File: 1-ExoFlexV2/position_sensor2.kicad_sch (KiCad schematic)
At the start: 21 parts, among them J103 Jumper, J104 Jumper, J105 Jumper, U73 Inverter, U74 Inverter, U75 Inverter, U76 AND Gate, U77 AND Gate, U78 Inverter

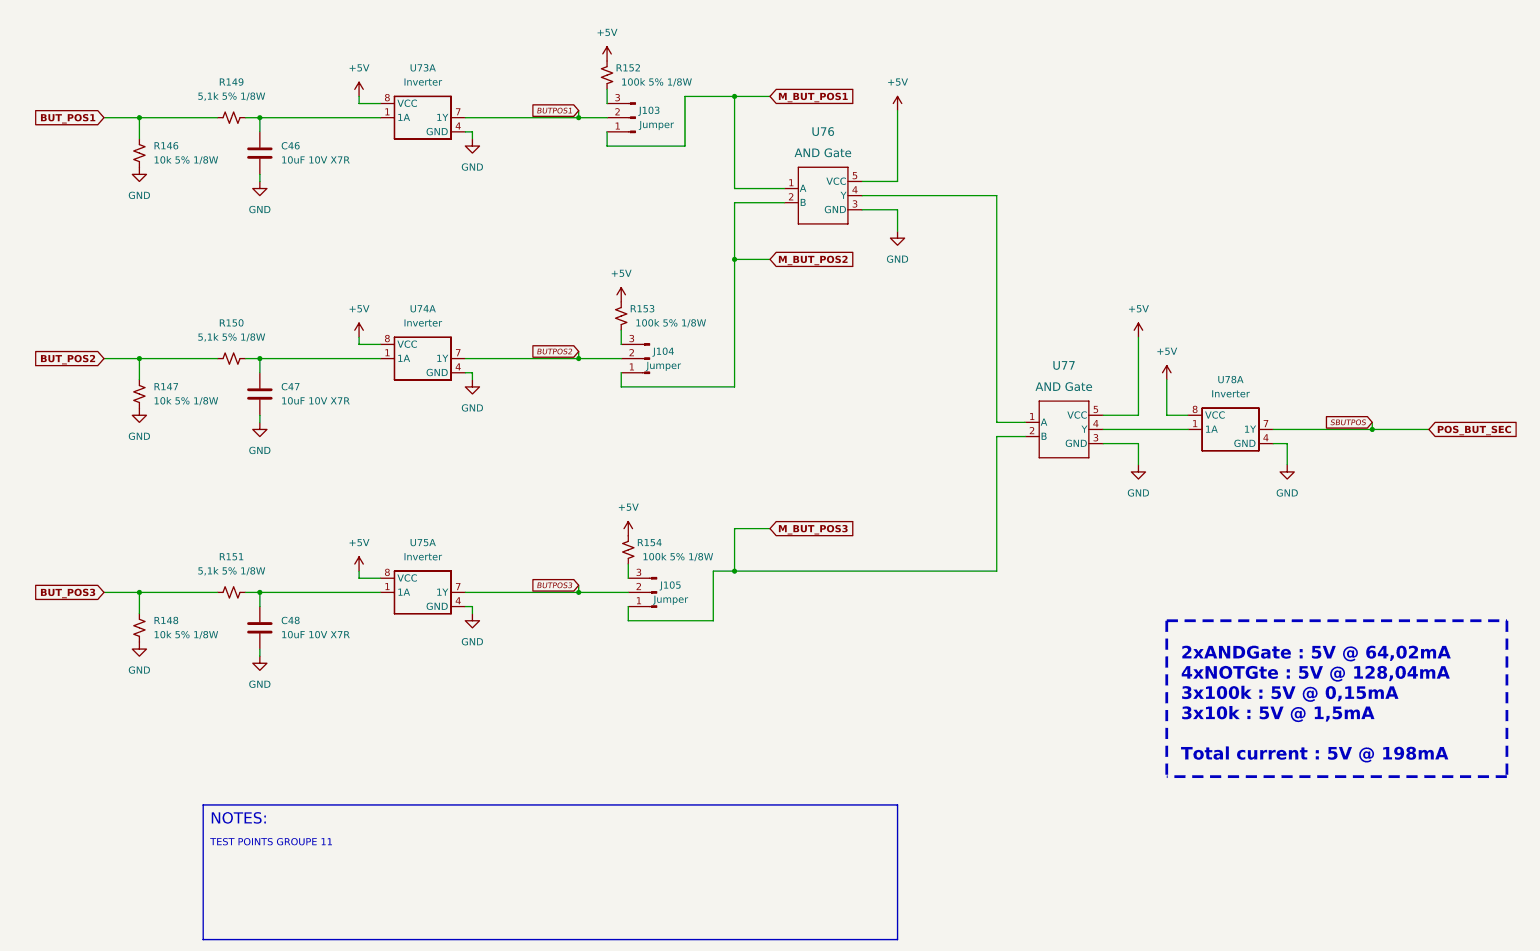
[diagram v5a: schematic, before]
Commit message: Finalisation 3
- Changement des régulateur de tension
- Retrait de test point inutile
- Changement de jumper mal positionner
- Ajout de Mounting holes et fiducial
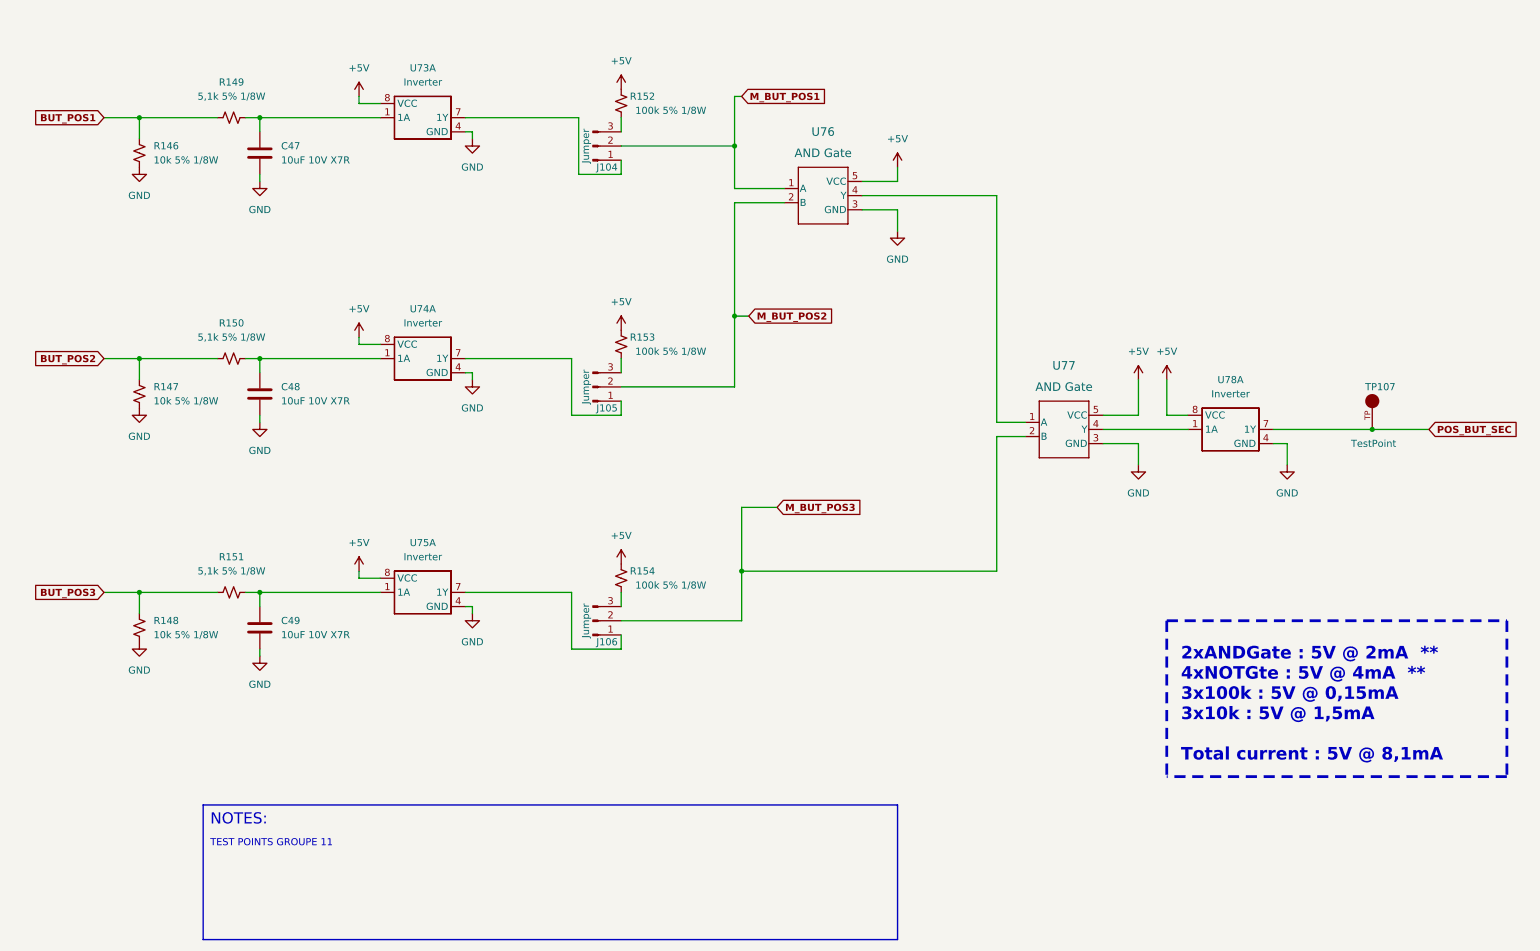
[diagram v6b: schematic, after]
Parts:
- added TP107: TestPoint, FootPrint:KEYSTONE_5005, symbol SymLib:5005
- J104: renamed from J103; footprint Connector_PinSocket_2.54mm:PinSocket_1x03_P2.54mm_Vertical -> Connector_PinHeader_2.54mm:PinHeader_1x03_P2.54mm_Vertical
- J105: renamed from J104; footprint Connector_PinSocket_2.54mm:PinSocket_1x03_P2.54mm_Vertical -> Connector_PinHeader_2.54mm:PinHeader_1x03_P2.54mm_Vertical
- J106: renamed from J105; footprint Connector_PinSocket_2.54mm:PinSocket_1x03_P2.54mm_Vertical -> Connector_PinHeader_2.54mm:PinHeader_1x03_P2.54mm_Vertical
- renumbered C46 to C47, C47 to C48, C48 to C49
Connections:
- net M_BUT_POS1: now also J104.2 (Pin_2); no longer J104.1 (Pin_1)
- net M_BUT_POS2: now also J105.2 (Pin_2); no longer J105.1 (Pin_1)
- net M_BUT_POS3: now also J106.2 (Pin_2); no longer J106.1 (Pin_1)
- net POS_BUT_SEC: now also TP107.TP
- net BUTPOS1: no longer names the net of U73.7 (1Y)
- net BUTPOS1: now also J104.1 (Pin_1); no longer J104.2 (Pin_2)
- net BUTPOS2: no longer names the net of U74.7 (1Y)
- net BUTPOS2: now also J105.1 (Pin_1); no longer J105.2 (Pin_2)
- net BUTPOS3: no longer names the net of U75.7 (1Y)
- net BUTPOS3: now also J106.1 (Pin_1); no longer J106.2 (Pin_2)
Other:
- note added: "2xANDGate : 5V @ 2mA ** 4xNOTGte : 5V @ 4mA ** 3x100k : 5V @ 0,15mA 3x10k : 5V @ 1,5mA Total current : 5V @ 8,1mA"
- note removed: "2xANDGate : 5V @ 64,02mA 4xNOTGte : 5V @ 128,04mA 3x100k : 5V @ 0,15mA 3x10k : 5V @ 1,5mA Total current : 5V @ 198mA"
- moved on the sheet: J104, J105, J106, R152, R153, R154

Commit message: Finalisation schéma FIN
- Changement des uméro pour les inverseurs
- Changement des connecteur et début de placement
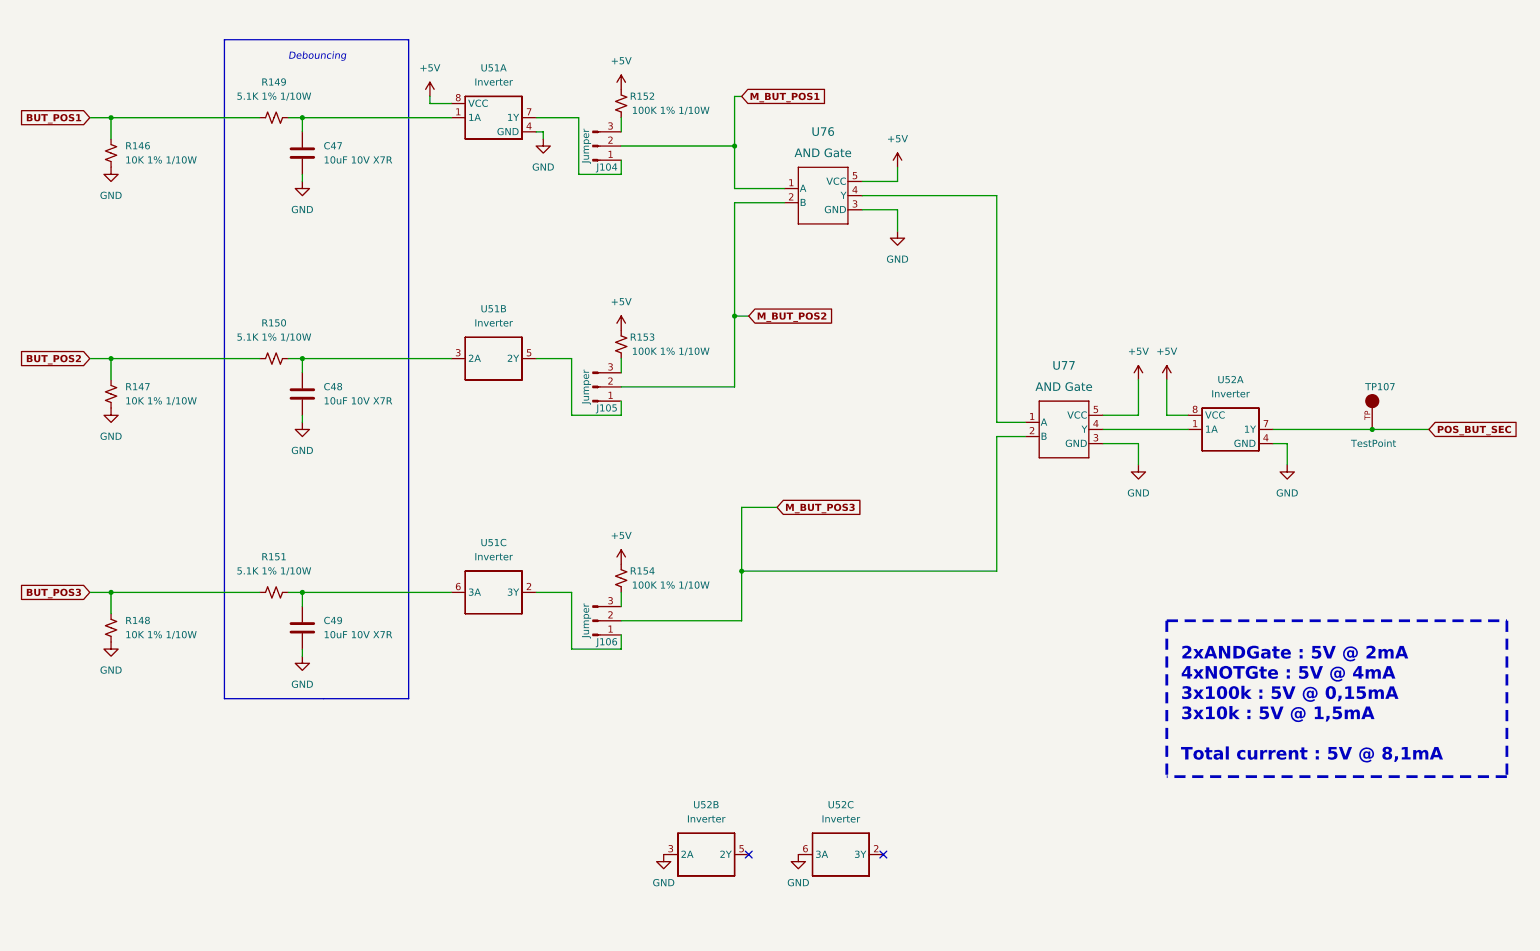
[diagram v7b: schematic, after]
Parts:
- removed U73, U74, U75, U78: Inverter, FootPrint:SN74LVC3G14DCUT, symbol SymLib:SN74LVC3G14DCUT_V2
- added U51, U52: Inverter, FootPrint:SN74LVC3G14DCUT, symbol SymLib:SN74LVC3G14DCUT_V2
- R146, R147, R148: value 10k 5% 1/8W -> 10K 1% 1/10W; footprint Resistor_SMD:R_0805_2012Metric -> Resistor_SMD:R_0603_1608Metric; DESCRIPTION 10 kOhms ±5% 0.125W, 1/8W Chip Resistor 0805 (2012 Metric) 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 -> 10 kOhms ±1% 0.1W, 1/10W Chip Resistor 0603 (1608 Metric) A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; PACKAGE 0805 (2012 Metric) -> 0603 (1608 Metric); PART NUMBER ERJ-6GEYJ103V -> ERJ-3EKF1002V
- R149, R150, R151: value 5,1k 5% 1/8W -> 5.1K 1% 1/10W; footprint Resistor_SMD:R_0805_2012Metric -> Resistor_SMD:R_0603_1608Metric; DESCRIPTION 5.1 kOhms ±5% 0.125W, 1/8W Chip Resistor 0805 (2012 Metric)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 -> 5.1 kOhms ±1% 0.1W, 1/10W Chip Resistor 0603 (1608 Metric) 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; PACKAGE 0805 (2012 Metric) -> 0603 (1608 Metric); PART NUMBER ERJ-6GEYJ512V -> ERJ-3EKF5101V
- R152, R153, R154: value 100k 5% 1/8W -> 100K 1% 1/10W; footprint Resistor_SMD:R_0805_2012Metric -> Resistor_SMD:R_0603_1608Metric; DESCRIPTION 100 kOhms ±5% 0.125W, 1/8W Chip Resistor 0805 (2012 Metric)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 -> 100 kOhms ±1% 0.1W, 1/10W Chip Resistor 0603 (1608 Metric) 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; PACKAGE 0805 (2012 Metric) -> 0603 (1608 Metric); PART NUMBER ERJ-6GEYJ104V -> ERJ-3EKF1003V
- TP107: NOTES (none) -> DO NOT POPULATE; PURCHASE-URL https://pricing.snapeda.com/search/part/5005/?ref=eda -> (none)
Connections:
- net +5V: now also U51.8 (VCC), U52.8 (VCC)
- net GND: now also U51.4 (GND), U52.3 (2A), U52.4 (GND), U52.6 (3A)
- net POS_BUT_SEC: now also U52.7 (1Y)
- net at C48.1, R150.2: now also U51.3 (2A)
- net at J105.1 (Pin_1): now also U51.5 (2Y)
- net at U77.4 (Y): now also U52.1 (1A)
- net at C49.1, R151.2: now also U51.6 (3A)
- net at J104.1 (Pin_1): now also U51.7 (1Y)
- net at C47.1, R149.2: now also U51.1 (1A)
- net at J106.1 (Pin_1): now also U51.2 (3Y)
- no-connect marks 0 -> 2
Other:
- note added: "2xANDGate : 5V @ 2mA 4xNOTGte : 5V @ 4mA 3x100k : 5V @ 0,15mA 3x10k : 5V @ 1,5mA Total current : 5V @ 8,1mA"
- note added: "Debouncing"
- note removed: "2xANDGate : 5V @ 2mA ** 4xNOTGte : 5V @ 4mA ** 3x100k : 5V @ 0,15mA 3x10k : 5V @ 1,5mA Total current : 5V @ 8,1mA"
- note removed: "NOTES:"
- note removed: "TEST POINTS GROUPE 11"
- moved on the sheet: C47, C48, C49, R146, R147, R148, R149, R150, R151

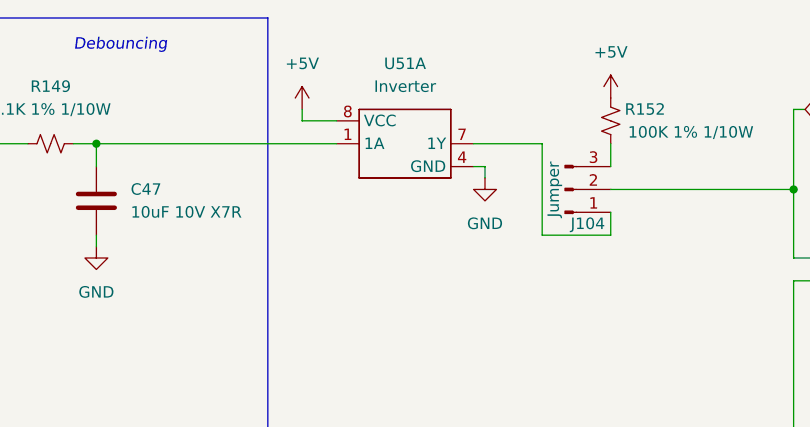
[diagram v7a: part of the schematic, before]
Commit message: Placement 1
- Placement de tous les connecteur
- Placement de tous les test point
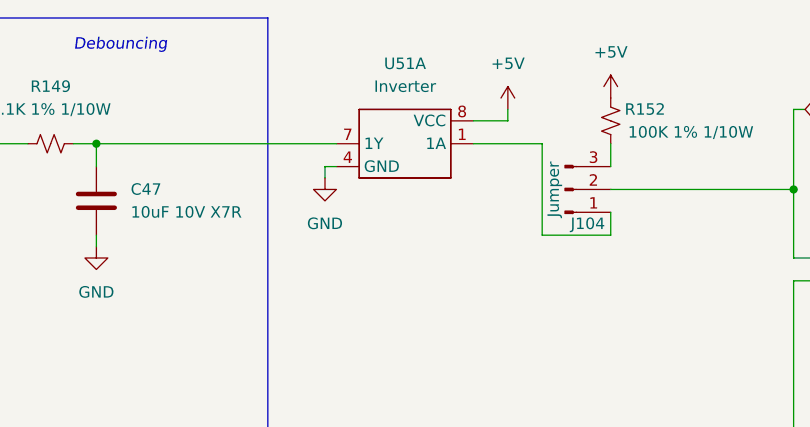
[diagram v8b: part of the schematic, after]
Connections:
- net at J104.1 (Pin_1): now also U51.1 (1A); no longer U51.7 (1Y)
- net at C47.1, R149.2: now also U51.7 (1Y); no longer U51.1 (1A)
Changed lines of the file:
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@@
     (stroke (width 0) (type default) (color 0 0 0 0))
   )
-  (wire (pts (xy 92.71 43.18) (xy 88.9 43.18))
+  (wire (pts (xy 107.95 43.18) (xy 111.76 43.18))
     (stroke (width 0) (type default) (color 0 0 0 0))
   )
@@
     (stroke (width 0) (type default) (color 0 0 0 0))
   )
-  (wire (pts (xy 88.9 43.18) (xy 88.9 41.91))
+  (wire (pts (xy 111.76 43.18) (xy 111.76 41.91))
     (stroke (width 0) (type default) (color 0 0 0 0))
   )
@@
     (stroke (width 0) (type default) (color 0 0 0 0))
   )
-  (wire (pts (xy 107.95 48.26) (xy 109.22 48.26))
+  (wire (pts (xy 92.71 48.26) (xy 91.44 48.26))
     (stroke (width 0) (type default) (color 0 0 0 0))
   )
@@
     (stroke (width 0) (type default) (color 0 0 0 0))
   )
-  (wire (pts (xy 109.22 49.53) (xy 109.22 48.26))
+  (wire (pts (xy 91.44 49.53) (xy 91.44 48.26))
     (stroke (width 0) (type default) (color 0 0 0 0))
   )
@@
     (pin "2")
   )
-  (symbol (lib_id "power:GND") (at 109.22 49.53 0) (unit 1)
-    (in_bom yes) (on_board yes) (fields_autoplaced)
-    (property "Reference" "#PWR0425" (id 0) (at 109.22 55.88 0)
-      (effects (font (size 1.27 1.27)) hide)
-    )
-    (property "Value" "GND" (id 1) (at 109.22 54.61 0))
-    (property "Footprint" "" (id 2) (at 109.22 49.53 0)
-      (effects (font (size 1.27 1.27)) hide)
-    )
-    (property "Datasheet" "" (id 3) (at 109.22 49.53 0)
-      (effects (font (size 1.27 1.27)) hide)
-    )
-    (pin "1")
-  )
-  (symbol (lib_id "power:+5V") (at 88.9 41.91 0) (unit 1)
-    (in_bom yes) (on_board yes) (fields_autoplaced)
-    (property "Reference" "#PWR0422" (id 0) (at 88.9 45.72 0)
-      (effects (font (size 1.27 1.27)) hide)
-    )
-    (property "Value" "+5V" (id 1) (at 88.9 36.83 0))
-    (property "Footprint" "" (id 2) (at 88.9 41.91 0)
-      (effects (font (size 1.27 1.27)) hide)
-    )
-    (property "Datasheet" "" (id 3) (at 88.9 41.91 0)
+  (symbol (lib_id "power:GND") (at 91.44 49.53 0) (mirror y) (unit 1)
+    (in_bom yes) (on_board yes) (fields_autoplaced)
+    (property "Reference" "#PWR0425" (id 0) (at 91.44 55.88 0)
+      (effects (font (size 1.27 1.27)) hide)
+    )
+    (property "Value" "GND" (id 1) (at 91.44 54.61 0))
+    (property "Footprint" "" (id 2) (at 91.44 49.53 0)
+      (effects (font (size 1.27 1.27)) hide)
+    )
+    (property "Datasheet" "" (id 3) (at 91.44 49.53 0)
+      (effects (font (size 1.27 1.27)) hide)
+    )
+    (pin "1")
+  )
+  (symbol (lib_id "power:+5V") (at 111.76 41.91 0) (mirror y) (unit 1)
+    (in_bom yes) (on_board yes) (fields_autoplaced)
+    (property "Reference" "#PWR0422" (id 0) (at 111.76 45.72 0)
+      (effects (font (size 1.27 1.27)) hide)
+    )
+    (property "Value" "+5V" (id 1) (at 111.76 36.83 0))
+    (property "Footprint" "" (id 2) (at 111.76 41.91 0)
+      (effects (font (size 1.27 1.27)) hide)
+    )
+    (property "Datasheet" "" (id 3) (at 111.76 41.91 0)
       (effects (font (size 1.27 1.27)) hide)
     )
@@
     (pin "1")
   )
-  (symbol (lib_id "SymLib:SN74LVC3G14DCUT_V2") (at 100.33 45.72 0) (unit 1)
+  (symbol (lib_id "SymLib:SN74LVC3G14DCUT_V2") (at 100.33 45.72 0) (mirror y) (unit 1)
     (in_bom yes) (on_board yes) (fields_autoplaced)
     (property "Reference" "U51" (id 0) (at 100.33 36.83 0))
     (property "Value" "Inverter" (id 1) (at 100.33 39.37 0))
-    (property "Footprint" "FootPrint:SN74LVC3G14DCUT" (id 2) (at 102.87 38.1 0)
-      (effects (font (size 1.27 1.27)) hide)
-    )
+    (property "Footprint" "FootPrint:SN74LVC3G14DCUT" (id 2) (at 97.79 38.1 0)
+      (effects (font (size 1.27 1.27)) hide)
+    )
